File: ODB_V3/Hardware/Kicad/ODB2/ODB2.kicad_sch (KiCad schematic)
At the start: 83 parts, among them U14 STM32F412ZGTx, Y1 ABM8G-25.000MHZ-18-D2Y-T

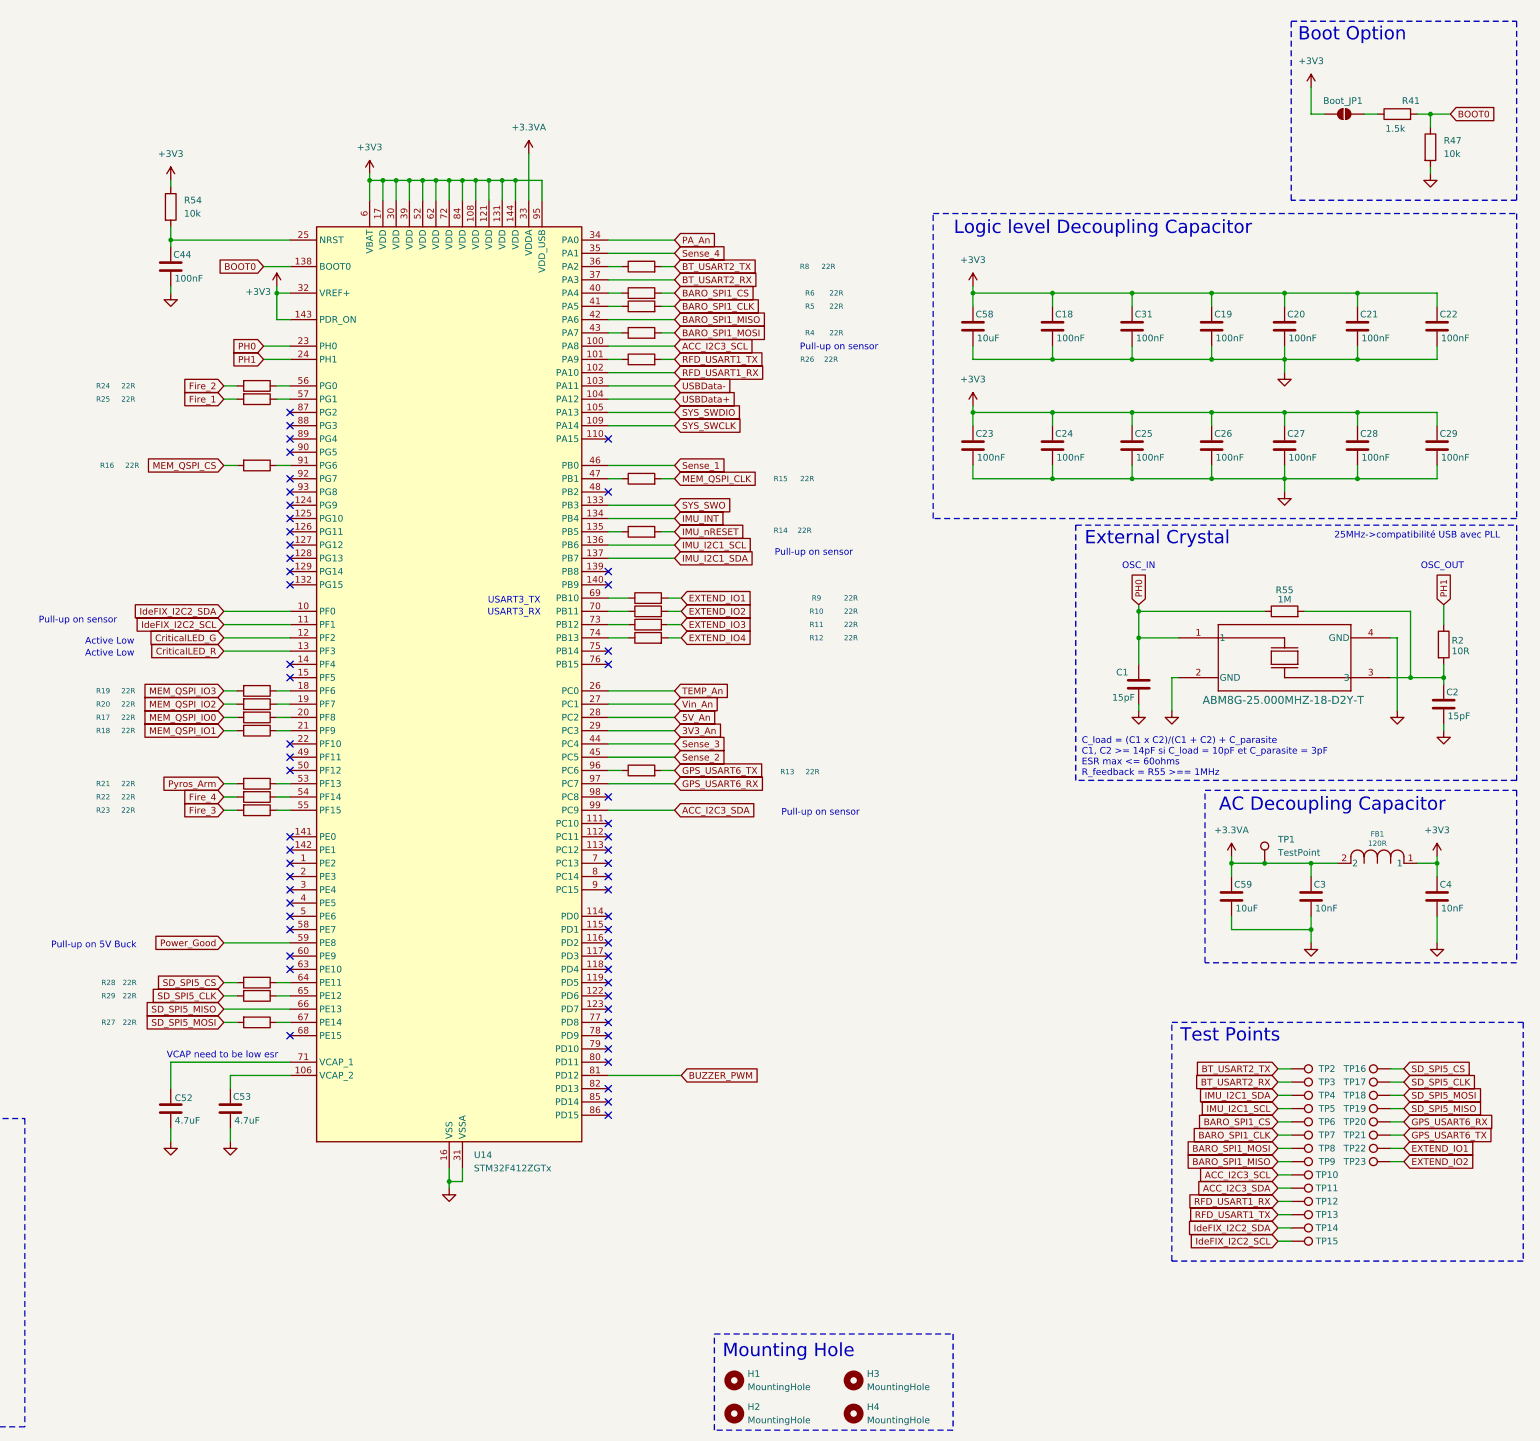
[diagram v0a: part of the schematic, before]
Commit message: wip : début refdes sur silkscreen
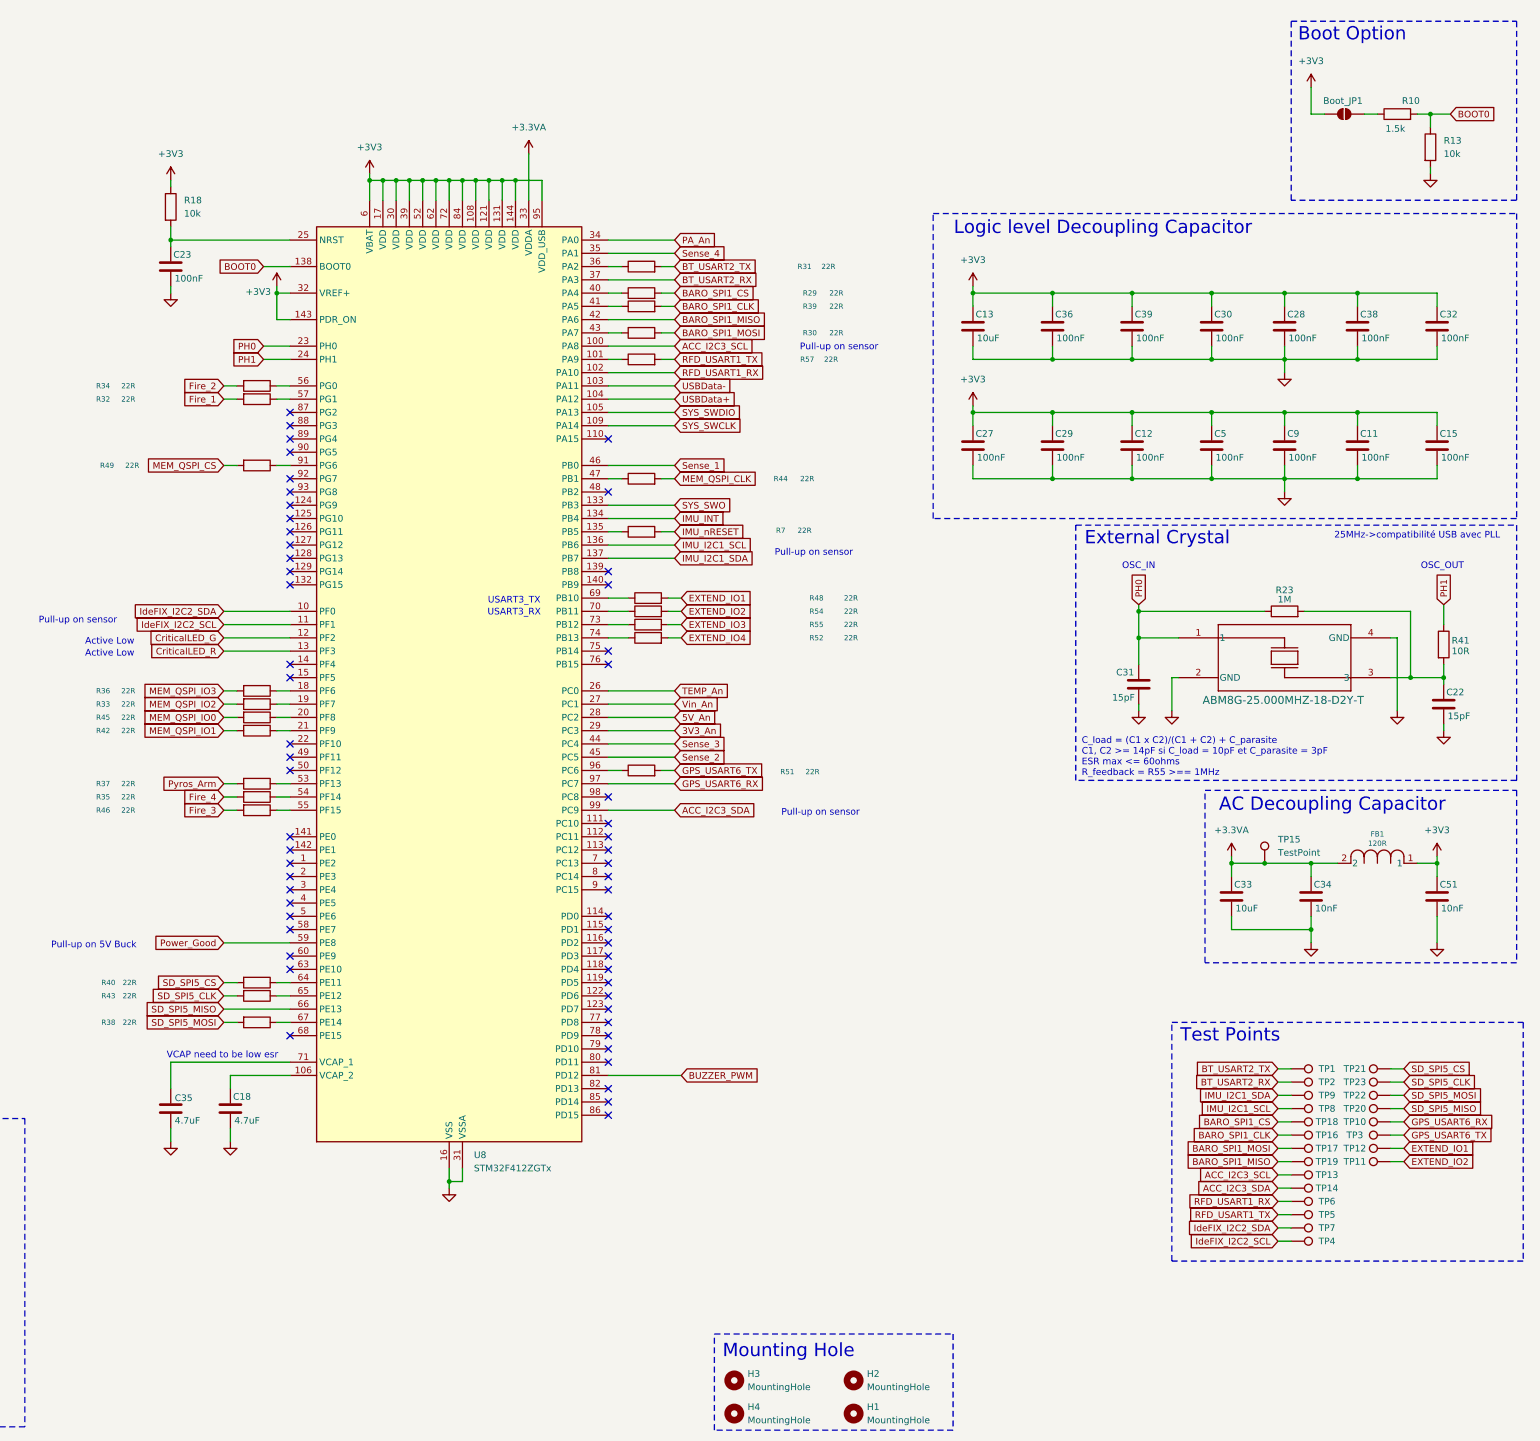
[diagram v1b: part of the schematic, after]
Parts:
- renumbered C28 to C11, C25 to C12, C58 to C13, C29 to C15, C53 to C18, C2 to C22, C44 to C23, C23 to C27, C20 to C28, C24 to C29, C19 to C30, C1 to C31, C22 to C32, C59 to C33, C3 to C34, C52 to C35, C18 to C36, C21 to C38, C31 to C39, C26 to C5, C4 to C51, C27 to C9, H4 to H1, H3 to H2, H1 to H3, H2 to H4, R41 to R10, R47 to R13, R54 to R18, R55 to R23, R6 to R29, R4 to R30, R8 to R31, R25 to R32, R20 to R33, R24 to R34, R22 to R35, R19 to R36, R21 to R37, R27 to R38, R5 to R39, R28 to R40, R2 to R41, R18 to R42, R29 to R43, R15 to R44, R17 to R45, R23 to R46, R9 to R48, R16 to R49, R13 to R51, R12 to R52, R10 to R54, R11 to R55, R26 to R57, R14 to R7, TP2 to TP1, TP20 to TP10, TP23 to TP11, TP22 to TP12, TP10 to TP13, TP11 to TP14, TP1 to TP15, TP7 to TP16, TP8 to TP17, TP6 to TP18, TP9 to TP19, TP3 to TP2, TP19 to TP20, TP16 to TP21, TP18 to TP22, TP17 to TP23, TP21 to TP3, TP15 to TP4, TP13 to TP5, TP12 to TP6, TP14 to TP7, TP5 to TP8, TP4 to TP9, U14 to U8

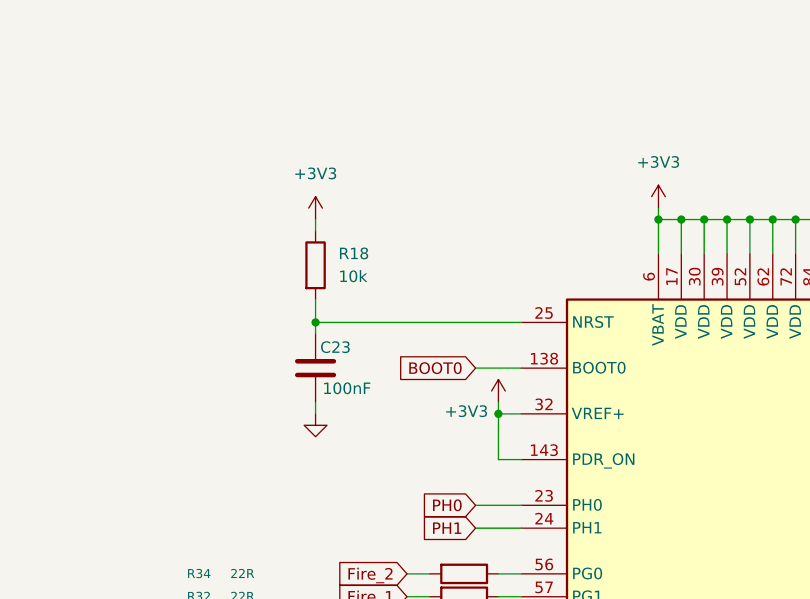
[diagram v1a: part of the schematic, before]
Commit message: wip: add nrst hardware stlink + change header 01x05->01x06
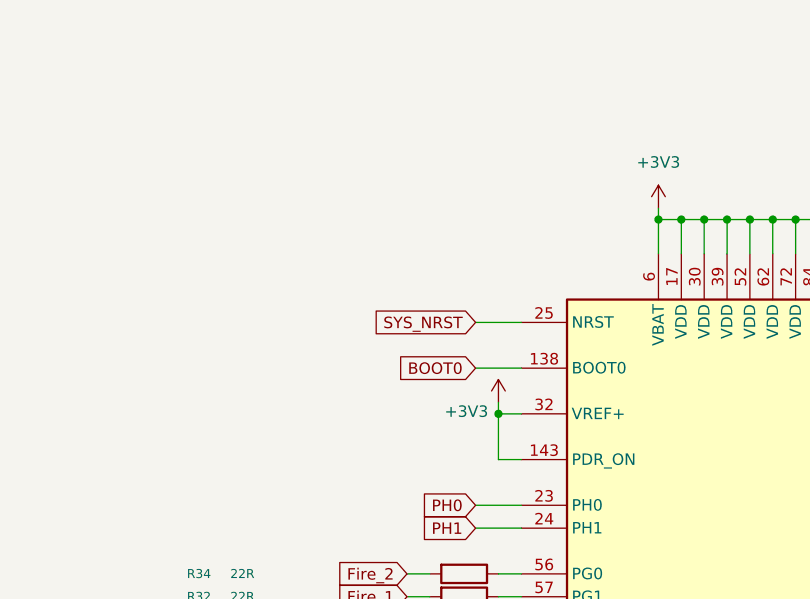
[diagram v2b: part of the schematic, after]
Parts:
- removed C23: 100nF, ODB:C_0402_1005Metric, symbol Device:C
- removed R18: 10k, Resistor_SMD:R_0603_1608Metric, symbol Device:R
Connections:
- net SYS_NRST: now reaches U8.25 (NRST)

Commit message: wip : fill all components in BOM
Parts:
- C11, C12, C15, C27, C28, C29, C30, C32, C36, C38, C39, C5, C9: DigiKey_Part_Number (none) -> 311-3342-1-ND
- C13, C33: DigiKey_Part_Number (none) -> 490-13248-1-ND
- C18, C35: DigiKey_Part_Number (none) -> 4988-NMC0603X5R475K6.3TRPFCT-ND
- C22, C31: DigiKey_Part_Number (none) -> 490-11191-1-ND
- C34, C51: DigiKey_Part_Number (none) -> 490-1313-1-ND
- R10: DigiKey_Part_Number (none) -> 408-1766-1-ND
- R13: DigiKey_Part_Number (none) -> 311-10.0KHRCT-ND
- R23: DigiKey_Part_Number (none) -> P1.00MLCT-ND
- R29, R30, R31, R32, R33, R34, R35, R36, R37, R38, R39, R40, R42, R43, R44, R45, R46, R48, R49, R51, R52, R54, R55, R57, R7: DigiKey_Part_Number (none) -> 311-22.0LRCT-ND
- R41: DigiKey_Part_Number (none) -> 541-10.0LCT-ND

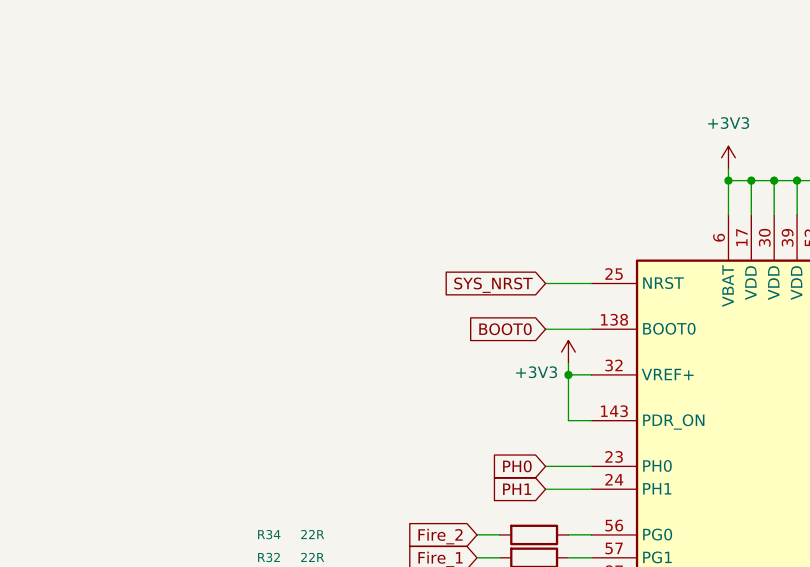
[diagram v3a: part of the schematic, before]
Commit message: wip : done filling BOM, fix silkscreen, fix NRST hardware
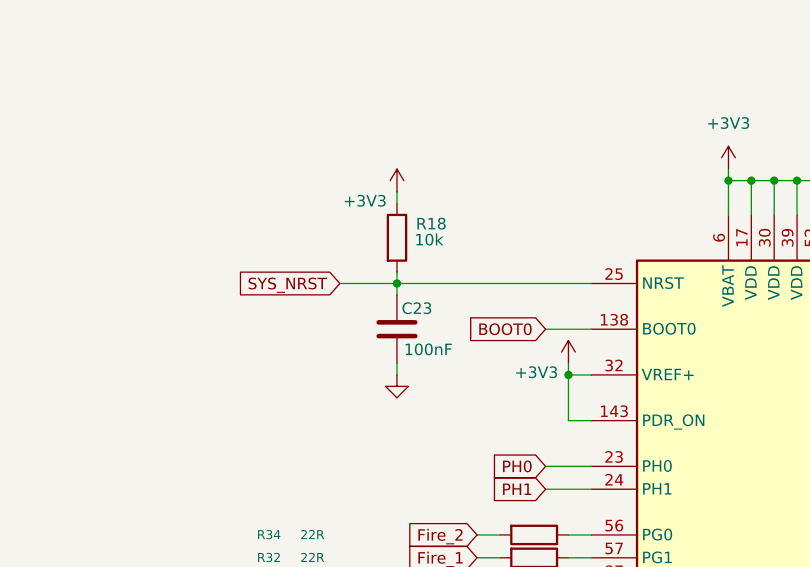
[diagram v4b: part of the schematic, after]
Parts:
- added C23: 100nF, ODB:C_0402_1005Metric, symbol Device:C
- added R18: 10k, Resistor_SMD:R_0603_1608Metric, symbol Device:R
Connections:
- net +3V3: now also R18.1
- net GND: now also C23.2
- net SYS_NRST: now also C23.1, R18.2

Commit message: wip : add MPN and fix footprints
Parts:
- C11, C12, C15, C23, C27, C28, C29, C30, C32, C36, C38, C39, C5, C9: Manufacturer_Part_Number (none) -> CC0402KRX5R9BB104
- C13, C33: Manufacturer_Part_Number (none) -> GRM188R6YA106MA73D
- C18, C35: Manufacturer_Part_Number (none) -> NMC0603X5R475K6.3TRPF
- C22, C31: Manufacturer_Part_Number (none) -> GJM1555C1H150FB01D
- C34, C51: Manufacturer_Part_Number (none) -> GRM155R71C103KA01D
- FB1: Manufacturer_Part_Number (none) -> 2508051217Y6
- R10: Manufacturer_Part_Number (none) -> URG1608L-152-L-T05
- R13, R18: Manufacturer_Part_Number (none) -> RC0603FR-0710KL
- R23: Manufacturer_Part_Number (none) -> ERJ-2RKF1004X
- R29, R30, R31, R32, R33, R34, R35, R36, R37, R38, R39, R40, R42, R43, R44, R45, R46, R48, R49, R51, R52, R54, R55, R57, R7: Manufacturer_Part_Number (none) -> RC0402FR-0722RL
- R41: Manufacturer_Part_Number (none) -> CRCW040210R0FKED
- U8: Manufacturer_Part_Number (none) -> STM32F412ZGT6
- Y1: Manufacturer_Part_Number (none) -> ABM8G-25.000MHZ-18-D2Y-T
